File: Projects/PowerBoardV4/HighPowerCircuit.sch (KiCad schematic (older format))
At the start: 17 parts, among them J1 Cell Voltage Sense, J10 5V_INT_PWR_BLK, J12 12V_INT_PWR_BLK, J2 BATT_PWR, J3 12V POWER SUPPLY, J5 BACK_EXT_24V, J7 MC_STACK_1, J8 MC_STACK_2, J9 24V_INT_PWR_BLK, Q1 IRF3205, Q2 IRF3205, Q3 BSS84

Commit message: Created netlist for PowerBoardV4, added footprints for Q1 and Q2
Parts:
- C1: footprint (none) -> Capacitors_ThroughHole:C_Radial_D5_L11_P2.5
- J10: footprint TerminalBlocks_Phoenix:TerminalBlock_Phoenix_PT-3.5mm_6pol -> Terminal_Blocks:TerminalBlock_Pheonix_PT-3.5mm_6pol
- J3: footprint (none) -> USST-footprints:R-6212P_14-34VDC-12VDC_Converter
- Q1, Q2: footprint TO_SOT_Packages_THT:TO-220-3_Vertical -> USST-footprints:TO-220-2_Vertical_Ver2
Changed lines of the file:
@@
 EESchema Schematic File Version 2
+LIBS:PowerBoardV4-rescue
 LIBS:power
 LIBS:device
 LIBS:switches
 LIBS:relays
-LIBS:motors
 LIBS:transistors
 LIBS:conn
@@
 F 0 "Q2" H 1600 4525 50  0000 L CNN
 F 1 "IRF3205" H 1600 4450 50  0000 L CNN
-F 2 "TO_SOT_Packages_THT:TO-220-3_Vertical" H 1600 4375 50  0001 L CIN
+F 2 "USST-footprints:TO-220-2_Vertical_Ver2" H 1600 4375 50  0001 L CIN
 F 3 "" H 1350 4450 50  0001 L CNN
 	1    1350 4450
@@
 F 0 "Q1" H 1600 3525 50  0000 L CNN
 F 1 "IRF3205" H 1600 3450 50  0000 L CNN
-F 2 "TO_SOT_Packages_THT:TO-220-3_Vertical" H 1600 3375 50  0001 L CIN
+F 2 "USST-footprints:TO-220-2_Vertical_Ver2" H 1600 3375 50  0001 L CIN
 F 3 "" H 1350 3450 50  0001 L CNN
 	1    1350 3450
@@
 U 1 1 5AA1D9C7
 P 1450 2850
+AR Path="/5AA1D9C7" Ref="Q3"  Part="1"
+AR Path="/5AA250C9/5AA1D9C7" Ref="Q3"  Part="1"
 F 0 "Q3" H 1650 2925 50  0000 L CNN
 F 1 "BSS84" H 1650 2850 50  0000 L CNN
@@
 F 0 "J10" H 3450 6800 50  0000 C CNN
 F 1 "5V_INT_PWR_BLK" H 3450 6100 50  0000 C CNN
-F 2 "TerminalBlocks_Phoenix:TerminalBlock_Phoenix_PT-3.5mm_6pol" H 3450 6500 50  0001 C CNN
+F 2 "Terminal_Blocks:TerminalBlock_Pheonix_PT-3.5mm_6pol" H 3450 6500 50  0001 C CNN
 F 3 "" H 3450 6500 50  0001 C CNN
 	1    3450 6500
@@
 F 0 "J3" H 1750 6675 50  0000 C CNN
 F 1 "12V POWER SUPPLY" H 1750 5375 50  0000 C CNN
-F 2 "" H 1750 6075 50  0001 C CNN
+F 2 "USST-footprints:R-6212P_14-34VDC-12VDC_Converter" H 1750 6075 50  0001 C CNN
 F 3 "" H 1750 6075 50  0001 C CNN
 	1    1750 6075
@@
 F 0 "C1" H 1335 6445 50  0000 L CNN
 F 1 "10uF" H 1335 6295 50  0000 L CNN
-F 2 "" H 1325 6375 50  0001 C CNN
+F 2 "Capacitors_ThroughHole:C_Radial_D5_L11_P2.5" H 1325 6375 50  0001 C CNN
 F 3 "" H 1325 6375 50  0001 C CNN
 	1    1325 6375

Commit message: editted R18 footprint and double checked Q1 and Q2 footprints
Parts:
- Q3: symbol BSS84 -> BSS84-RESCUE-PowerBoardV4
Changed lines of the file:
@@
 $EndComp
 $Comp
-L BSS84 Q3
+L BSS84-RESCUE-PowerBoardV4 Q3
 U 1 1 5AA1D9C7
 P 1450 2850

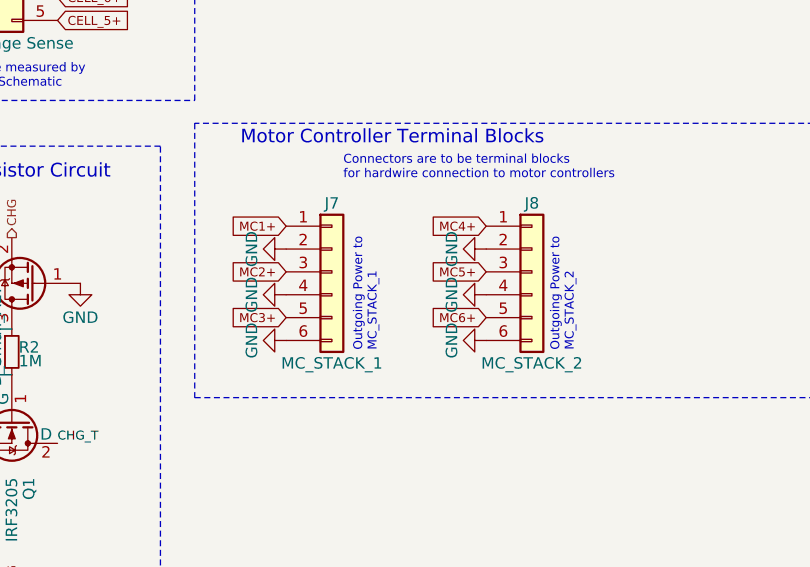
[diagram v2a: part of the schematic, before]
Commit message: modified the PowerBoard V4 schematic, left a comment by the usb connector
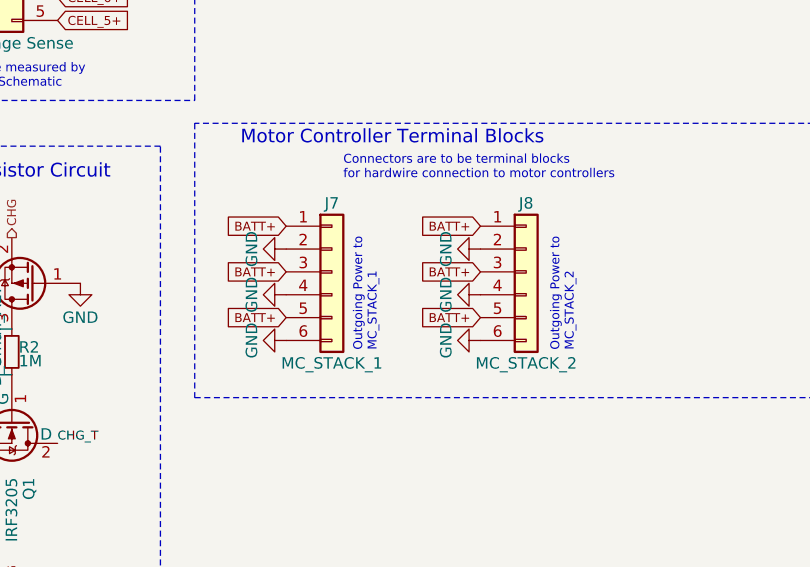
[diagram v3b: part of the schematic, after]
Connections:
- net MC1+ is gone; now on net BATT+: J7.1 (Pin_1)
- net MC2+ is gone; now on net BATT+: J7.3 (Pin_3)
- net MC3+ is gone; now on net BATT+: J7.5 (Pin_5)
- net MC4+ is gone; now on net BATT+: J8.1 (Pin_1)
- net MC5+ is gone; now on net BATT+: J8.3 (Pin_3)
- net MC6+ is gone; now on net BATT+: J8.5 (Pin_5)
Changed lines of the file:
@@
 LIBS:switches
 LIBS:relays
+LIBS:motors
 LIBS:transistors
 LIBS:conn
@@
 Text Notes 2950 3150 1    39   ~ 0
 Outgoing Power to \nMC_STACK_1\n
-Text GLabel 2550 2600 0    39   Input ~ 0
-MC1+
-Text GLabel 2550 2800 0    39   Input ~ 0
-MC2+
-Text GLabel 2550 3000 0    39   Input ~ 0
-MC3+
-$Comp
-L Conn_01x06 J8
-U 1 1 5AA22202
-P 3625 2800
-F 0 "J8" H 3625 3100 50  0000 C CNN
-F 1 "MC_STACK_2" H 3625 2400 50  0000 C CNN
-F 2 "USST-footprints:TerminalBlock_Pheonix_PT-5mm_6pol" H 3625 2800 50  0001 C CNN
-F 3 "" H 3625 2800 50  0001 C CNN
-	1    3625 2800
-	1    0    0    -1
-$EndComp
 Text Notes 3875 3150 1    39   ~ 0
 Outgoing Power to \nMC_STACK_2\n\n
-Text GLabel 3425 2600 0    39   Input ~ 0
-MC4+
-Text GLabel 3425 2800 0    39   Input ~ 0
-MC5+
-Text GLabel 3425 3000 0    39   Input ~ 0
-MC6+
 Wire Notes Line
 	550  2250 550  5050
@@
 	0    1    1    0
 $EndComp
+Text GLabel 2550 2600 0    39   Input ~ 0
+BATT+
+Text GLabel 2550 2800 0    39   Input ~ 0
+BATT+
+Text GLabel 2550 3000 0    39   Input ~ 0
+BATT+
+$Comp
+L Conn_01x06 J8
+U 1 1 5B44454C
+P 3600 2800
+F 0 "J8" H 3600 3100 50  0000 C CNN
+F 1 "MC_STACK_2" H 3600 2400 50  0000 C CNN
+F 2 "USST-footprints:TerminalBlock_Pheonix_PT-5mm_6pol" H 3600 2800 50  0001 C CNN
+F 3 "" H 3600 2800 50  0001 C CNN
+	1    3600 2800
+	1    0    0    -1
+$EndComp
+Text GLabel 3400 2600 0    39   Input ~ 0
+BATT+
+Text GLabel 3400 2800 0    39   Input ~ 0
+BATT+
+Text GLabel 3400 3000 0    39   Input ~ 0
+BATT+
 $Comp
 L GND #PWR019
-U 1 1 5B2EE339
-P 3425 3100
-F 0 "#PWR019" H 3425 2850 50  0001 C CNN
-F 1 "GND" H 3425 2950 50  0000 C CNN
-F 2 "" H 3425 3100 50  0001 C CNN
-F 3 "" H 3425 3100 50  0001 C CNN
-	1    3425 3100
+U 1 1 5B444762
+P 3400 2700
+F 0 "#PWR019" H 3400 2450 50  0001 C CNN
+F 1 "GND" H 3400 2550 50  0000 C CNN
+F 2 "" H 3400 2700 50  0001 C CNN
+F 3 "" H 3400 2700 50  0001 C CNN
+	1    3400 2700
 	0    1    1    0
 $EndComp
 $Comp
 L GND #PWR020
-U 1 1 5B2EE377
-P 3425 2900
-F 0 "#PWR020" H 3425 2650 50  0001 C CNN
-F 1 "GND" H 3425 2750 50  0000 C CNN
-F 2 "" H 3425 2900 50  0001 C CNN
-F 3 "" H 3425 2900 50  0001 C CNN
-	1    3425 2900
+U 1 1 5B4447A0
+P 3400 2900
+F 0 "#PWR020" H 3400 2650 50  0001 C CNN
+F 1 "GND" H 3400 2750 50  0000 C CNN
+F 2 "" H 3400 2900 50  0001 C CNN
+F 3 "" H 3400 2900 50  0001 C CNN
+	1    3400 2900
 	0    1    1    0
 $EndComp
 $Comp
 L GND #PWR021
-U 1 1 5B2EE3B5
-P 3425 2700
-F 0 "#PWR021" H 3425 2450 50  0001 C CNN
-F 1 "GND" H 3425 2550 50  0000 C CNN
-F 2 "" H 3425 2700 50  0001 C CNN
-F 3 "" H 3425 2700 50  0001 C CNN
-	1    3425 2700
-	0    1    1    0
-$EndComp
+U 1 1 5B4447DE
+P 3400 3100
+F 0 "#PWR021" H 3400 2850 50  0001 C CNN
+F 1 "GND" H 3400 2950 50  0000 C CNN
+F 2 "" H 3400 3100 50  0001 C CNN
+F 3 "" H 3400 3100 50  0001 C CNN
+	1    3400 3100
+	0    1    1    0
+$EndComp

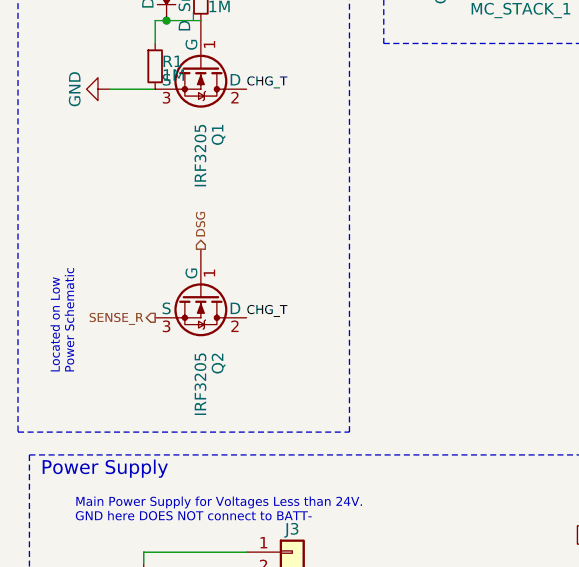
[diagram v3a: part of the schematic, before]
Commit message: Review of Schematic to Datasheet
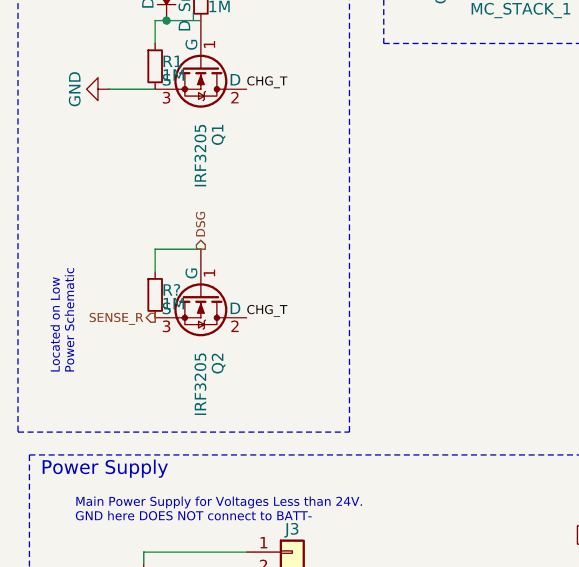
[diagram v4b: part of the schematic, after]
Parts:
- removed Q3: BSS84, TO_SOT_Packages_SMD:SOT-23, symbol BSS84-RESCUE-PowerBoardV4
- added Q3: BSS84, TO_SOT_Packages_SMD:SOT-23, symbol BSS84
- added R?: 1M, Resistors_SMD:R_0603, symbol R_Small
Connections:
- net CHG: now also Q3.2 (S)
- net DSG: now also R?.1
- net GND: now also Q3.1 (G)
- net SENSE_R: now also R?.2
- net at D1.2 (A), R2.1: now also Q3.3 (D)
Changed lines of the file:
@@
 $Descr A4 11693 8268
 encoding utf-8
-Sheet 2 3
+Sheet 1 3
 Title ""
 Date ""
@@
 	1    1350 3450
 	0    1    1    0
-$EndComp
-$Comp
-L BSS84-RESCUE-PowerBoardV4 Q3
-U 1 1 5AA1D9C7
-P 1450 2850
-AR Path="/5AA1D9C7" Ref="Q3"  Part="1"
-AR Path="/5AA250C9/5AA1D9C7" Ref="Q3"  Part="1"
-F 0 "Q3" H 1650 2925 50  0000 L CNN
-F 1 "BSS84" H 1650 2850 50  0000 L CNN
-F 2 "TO_SOT_Packages_SMD:SOT-23" H 1650 2775 50  0001 L CIN
-F 3 "" H 1450 2850 50  0001 L CNN
-	1    1450 2850
-	-1   0    0    1
 $EndComp
 $Comp
@@
 	0    1    1    0
 $EndComp
+$Comp
+L R_Small R?
+U 1 1 5B4A3D42
+P 1150 4450
+F 0 "R?" H 1180 4470 50  0000 L CNN
+F 1 "1M" H 1180 4410 50  0000 L CNN
+F 2 "Resistors_SMD:R_0603" H 1150 4450 50  0001 C CNN
+F 3 "" H 1150 4450 50  0001 C CNN
+	1    1150 4450
+	1    0    0    -1
+$EndComp
+Wire Wire Line
+	1150 4350 1150 4250
+Wire Wire Line
+	1150 4250 1350 4250
+$Comp
+L BSS84 Q3
+U 1 1 5B4A3F79
+P 1450 2850
+F 0 "Q3" H 1650 2925 50  0000 L CNN
+F 1 "BSS84" H 1650 2850 50  0000 L CNN
+F 2 "TO_SOT_Packages_SMD:SOT-23" H 1650 2775 50  0001 L CIN
+F 3 "" H 1450 2850 50  0001 L CNN
+	1    1450 2850
+	-1   0    0    1
+$EndComp
 $EndSCHEMATC

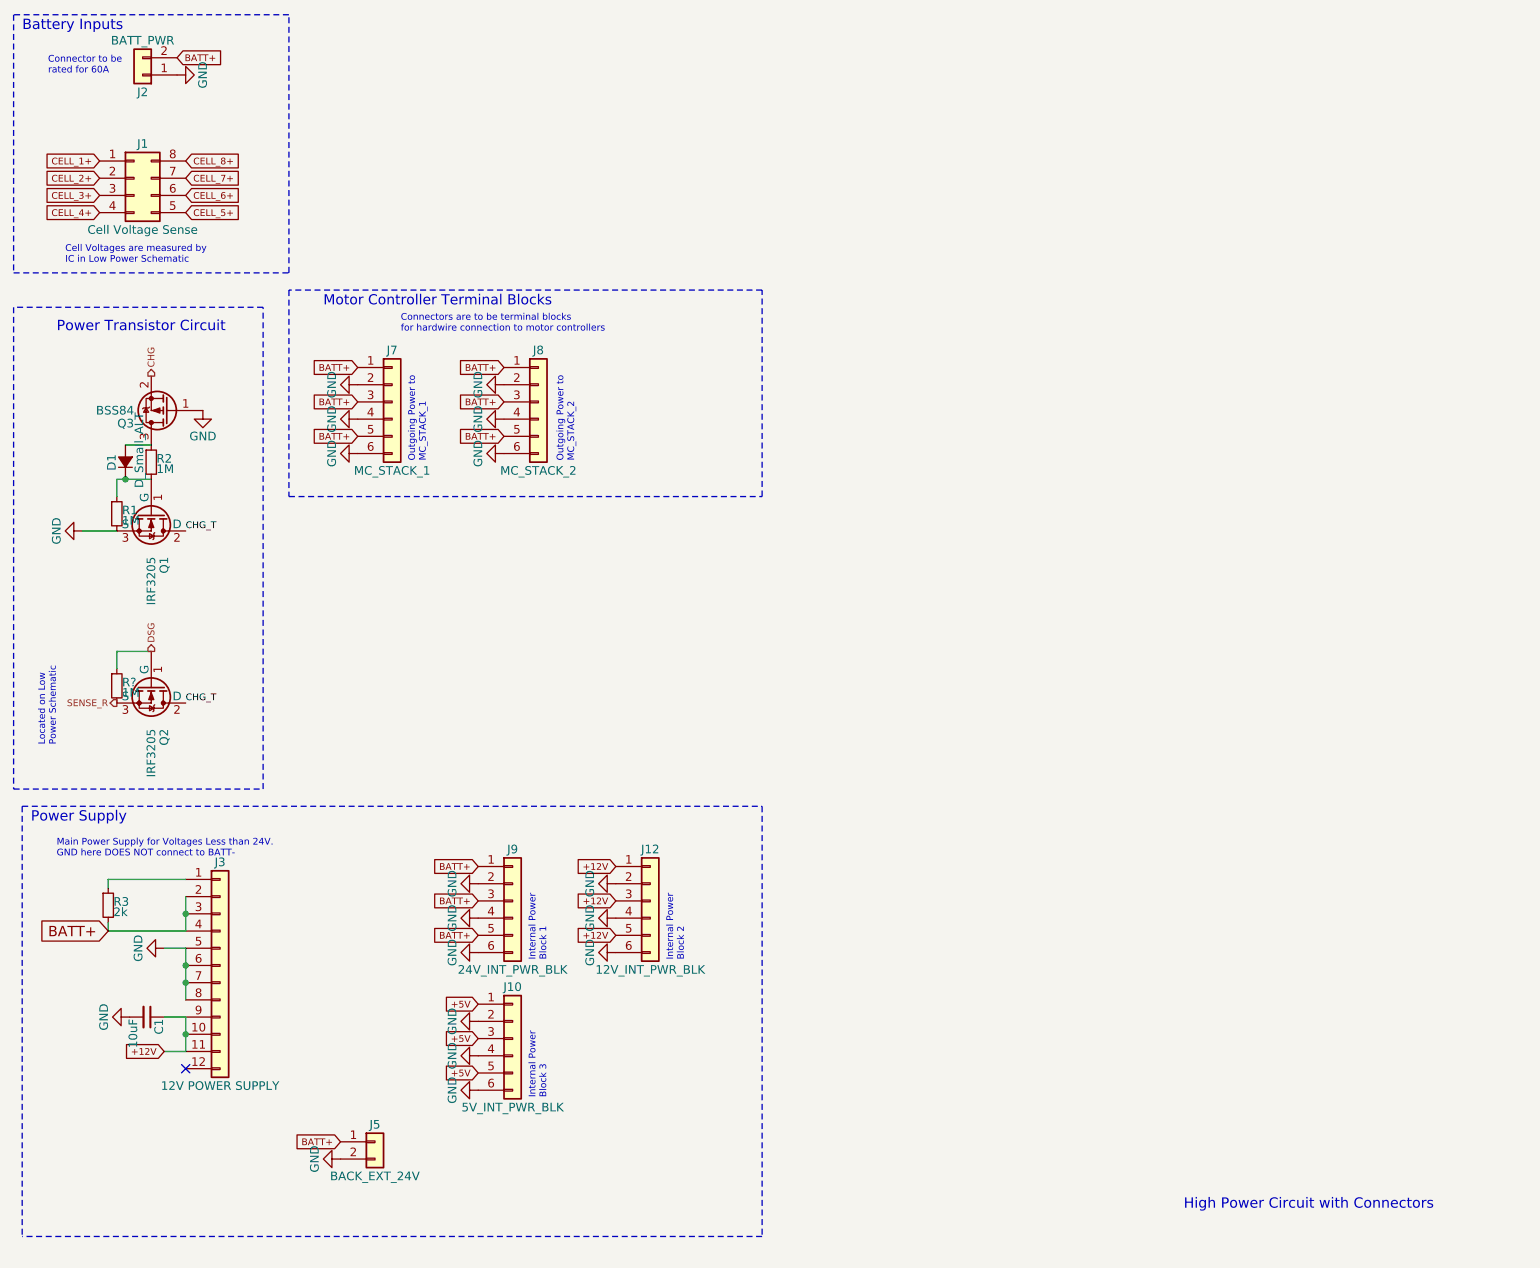
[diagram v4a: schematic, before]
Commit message: Complete 1st draft for power board v4
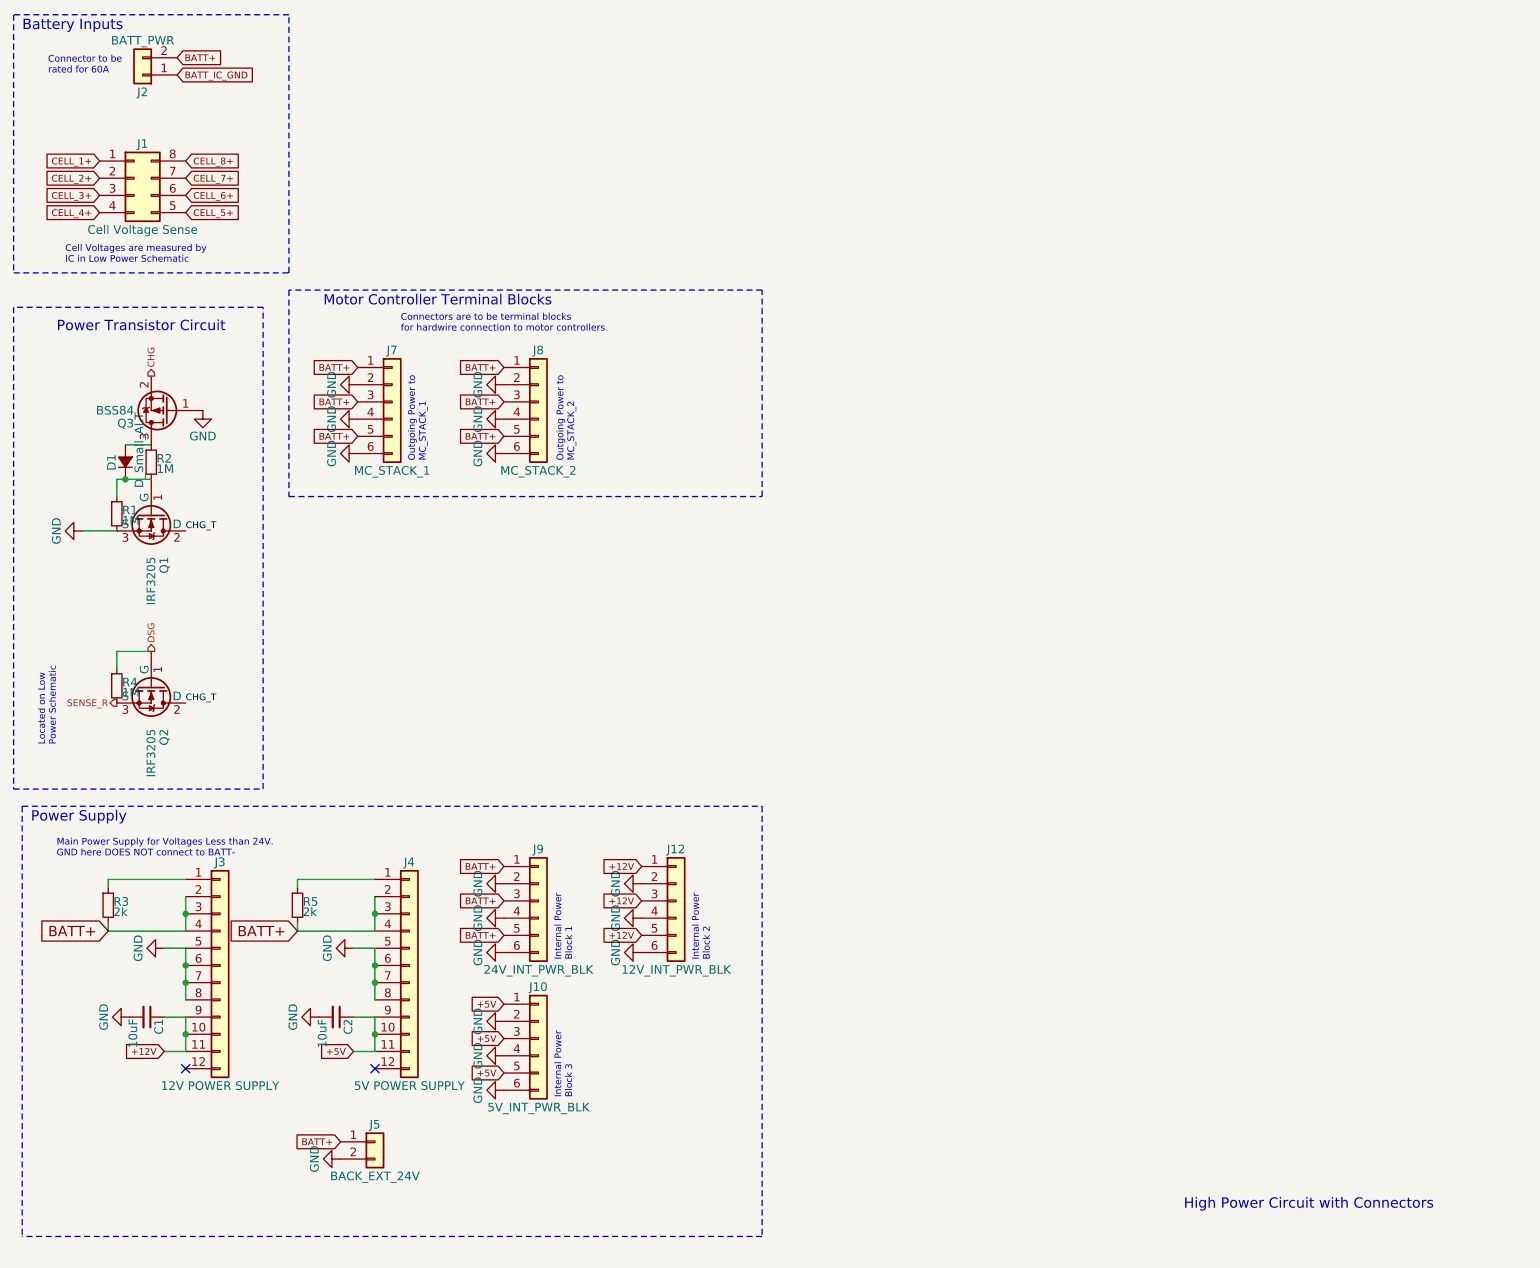
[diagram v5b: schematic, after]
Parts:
- added C2: 10uF, Capacitors_ThroughHole:C_Radial_D5_L11_P2.5, symbol C_Small
- added J4: 5V POWER SUPPLY, USST-footprints:SIP12_R-7xxx, symbol Conn_01x12
- added R5: 2k, Resistors_SMD:R_0603, symbol R_Small
- D1: footprint Diodes_SMD:D_SOD-323F -> Diodes_SMD:D_0603
- Q1, Q2: footprint USST-footprints:TO-220-2_Vertical_Ver2 -> USST-footprints:TO-220AB
- R3: footprint (none) -> Resistors_SMD:R_0603
- gave numbers to parts that had none: 1
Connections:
- net +5V: now also C2.1, J4.10 (Pin_10), J4.11 (Pin_11), J4.9 (Pin_9)
- net BATT+: now also J4.2 (Pin_2), J4.3 (Pin_3), J4.4 (Pin_4), R5.2
- net GND: now also C2.2, J4.5 (Pin_5), J4.6 (Pin_6), J4.7 (Pin_7), J4.8 (Pin_8); no longer J2.1 (Pin_1)
- new net: J4.1 (Pin_1), R5.1
- new net BATT_IC_GND: J2.1 (Pin_1)
- no-connect marks 1 -> 2
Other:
- moved on the sheet: J10, J12, J9
